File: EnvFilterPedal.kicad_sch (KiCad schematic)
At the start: 19 parts, among them U101 TL074

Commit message: schematic 1st pass
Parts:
- added C105, C106, C108, C109, C114, C115: 100n, symbol Device:C
- added C107: 4n7, symbol Device:C
- added C110, C112, C117, C118: 1n, symbol Device:C
- added C111, C113, C116, C119, C120: 1u, symbol Device:C
- added C121: 100u, Capacitor_THT:CP_Radial_D5.0mm_P2.00mm, symbol Device:C_Polarized_US
- added C122: 470p, Capacitor_SMD:C_0805_2012Metric, symbol Device:C
- added C123, C124: 470u, Capacitor_THT:CP_Radial_D5.0mm_P2.00mm, symbol Device:C_Polarized_US
- added D105, D106: 1N4148W, Diode_SMD:D_SOD-123, symbol Diode:1N4148W
- added D107: PMEG3030, Diode_SMD:D_SOD-123, symbol Device:D_Schottky
- added L101: 68uH, Inductor_SMD:L_TDK_VLS6045EX_VLS6045AF, symbol Device:L
- added Q101, Q102: BC857, Package_TO_SOT_SMD:SOT-23, symbol Transistor_BJT:BC857
- added R110, R111: 15k, symbol Device:R_US
- added R112, R113, R145, R146: 100k, symbol Device:R_US
- added R114: 2k2, symbol Device:R_US
- added R115: 470k, symbol Device:R_US
- added R116, R117, R126, R130, R131, R139: 4k7, symbol Device:R_US
- added R118, R128, R132, R140: 22k, symbol Device:R_US
- added R119, R120, R123, R127, R133, R138, R143, R144: 33k, symbol Device:R_US
- added R121, R122, R124, R125, R134, R135, R136, R137: 1k, symbol Device:R_US
- added R129: 10k, symbol Device:R_US
- added R141, R142: 47k, symbol Device:R_US
- added R147: 470, symbol Device:R_US
- added R148: 0.24R, Resistor_SMD:R_0805_2012Metric, symbol Device:R_US
- added R149: 51k, Resistor_SMD:R_0805_2012Metric, symbol Device:R_US
- added R150: 8k2, Resistor_SMD:R_0805_2012Metric, symbol Device:R_US
- added RV102, RV103, RV104: 10kB, symbol Device:R_Potentiometer_US
- added RV105: 100kB, symbol Device:R_Potentiometer_US
- added RV106: 100kA, symbol Device:R_Potentiometer_US
- added U102: TL074, symbol Amplifier_Operational:TL074
- added U103, U104: LM13700, symbol Amplifier_Operational:LM13700
- added U105: AZ34063U, Package_SO:SO-8_3.9x4.9mm_P1.27mm, symbol Regulator_Switching:AZ34063U
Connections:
- net +9V: now also C105.1, C108.1, C114.1, C121.1, R110.1, R148.1, U102.4 (V+), U103.11 (V+), U104.11 (V+), U105.6 (VCC)
- net -9V: now also C106.1, C109.1, C115.1, C122.2, C123.2, C124.2, D107.2 (A), R111.2, R115.2, R118.2, R128.2, R132.2, R140.2, R150.2, U102.11 (V-), U103.6 (V-), U104.6 (V-), U105.4 (GND)
- net ENV: now also RV102.1
- net FX_IN: now also C116.1, C117.2; no longer C103.1
- net GND: now also C105.2, C106.2, C108.2, C109.2, C112.2, C114.2, C115.2, C121.2, C123.1, C124.1, L101.2, Q101.1 (B), R114.2, R121.1, R122.1, R124.1, R125.1, R130.2, R134.1, R135.1, R136.1, R137.1, R146.1, R149.1, RV102.3, RV104.1, RV105.2, RV106.1, U102.12 (+), U102.5 (+)
- new net: R113.1, RV103.2
- new net: Q102.1 (B), R112.2, R113.2, R114.1
- new net: R131.2, U104.16
- new net: R133.1, R135.2, U104.13 (-)
- new net: R141.2, R143.1, RV105.1
- new net: R143.2, R144.2, R145.1, U102.13 (-)
- new net: C117.1, U104.10, U104.12
- new net: C119.1, R132.1, U104.9
- new net: C110.1, U103.5, U103.7
- new net: C110.2, D105.2 (A), D106.1 (K), R129.1, U102.8
- new net: C111.2, R119.2, R123.1
- new net: R123.2, R124.2, R127.1, U103.13 (-)
- new net: RV104.2, U102.10 (+)
- new net: R136.2, R138.1, U104.4 (-)
- new net: D105.1 (K), D106.2 (A), R129.2, R130.1, U102.9 (-)
- new net: C116.2, R120.1
- new net: R119.1, R120.2, R121.2, U103.4 (-)
- new net: C107.2, Q102.3 (C), R115.1, U102.6 (-)
- new net: C107.1, R116.2, U102.7
- new net: R112.1, U102.1, U102.2 (-)
- new net: RV102.2, U102.3 (+)
- new net: R126.1, U103.16
- new net: R146.2, R147.1, RV106.2
- new net: R145.2, RV106.3, U102.14
- new net: R142.2, R144.1, RV105.3
- new net: C112.1, U103.10, U103.12
- new net: R134.2, U104.14 (+)
- new net: Q101.2 (E), Q102.2 (E), R116.1
- new net: R139.2, U104.1
- new net: R137.2, U104.3 (+)
- new net: C118.1, U104.5, U104.7
- new net: R110.2, RV103.1
- new net: C120.1, R140.1, U104.8
- new net: C113.1, R128.1, U103.9
- new net: R117.1, U103.1
- new net: R122.2, U103.3 (+)
- new net: C111.1, R118.1, U103.8
- new net: R149.2, R150.1, U105.5 (FB)
- new net: R125.2, U103.14 (+)
- new net: R111.1, RV103.3
- new net: C122.1, U105.3 (CAP)
- new net ENV_IN: C103.1
- new net FX_OUT: R147.2
- new net HP1: C118.2, C119.2, R133.2
- new net HP_OUT: C120.2, R138.2, R141.1
- new net Iabc: Q101.3 (C), R117.2, R126.2, R131.1, R139.1
- new net LP_OUT: C113.2, R127.2, R142.1, RV104.3
- new net SWC: R148.2, U105.1 (SWC), U105.7 (Sense), U105.8 (DRC)
- new net SWE: D107.1 (K), L101.1, U105.2 (SWE)
- no-connect marks 0 -> 4
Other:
- note added: "Cutoff freq."
- note added: "Depth"
- note added: "Filter Mix"
- note added: "High Pass Section"
- note added: "Low Pass Section"
- note added: "OTA control current source"
- note added: "Resonance"
- note added: "Volume"

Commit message: footprints assigned
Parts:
- C101, C102, C103, C104, C105, C106, C107, C108, C109, C110, C111, C112, C113, C114, C115, C116, C117, C118, C119, C120: footprint (none) -> Capacitor_SMD:C_0805_2012Metric
- R101, R102, R103, R104, R105, R106, R107, R108, R109, R110, R111, R112, R113, R114, R115, R116, R117, R118, R119, R120, R121, R122, R123, R124, R125, R126, R127, R128, R129, R130, R131, R132, R133, R134, R135, R136, R137, R138, R139, R140, R141, R142, R143, R144, R145, R146, R147: footprint (none) -> Resistor_SMD:R_0805_2012Metric
- RV101, RV102, RV103, RV104, RV105, RV106: footprint (none) -> Potentiometer_THT:Potentiometer_Alpha_RV16AF_42_VeryLong
- U101, U102: footprint (none) -> Package_SO:SOIC-14_3.9x8.7mm_P1.27mm
- U103, U104: footprint (none) -> Package_SO:SOIC-16_3.9x9.9mm_P1.27mm
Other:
- note added: "Inverting SMPS"
- note added: "NOTE: this filter is based on the 2-pole resonant filter from my poly synth which in turn is based on the Korg MS-20 filter. I've swapped the op-amp current to voltage stages from those designs in favor of the LM13700's built-in darlington buffers. If spice can be trusted this circuit is almost identical in practice."
- note added: "Output Mixer"
- moved on the sheet: C121, C122, C123, C124, D107, L101, R148, R149, R150, U105

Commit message: rev 1 gerber
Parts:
- added C125: 10n, Capacitor_SMD:C_0805_2012Metric, symbol Device:C
- added D108: LED, LED_THT:LED_D3.0mm, symbol Device:LED
- added J101: ScopeGroundLoop, Connector:THT_GND_WIRE, symbol Connector:ScopeGroundLoop
- added J102: IO, Connector_PinHeader_2.54mm:PinHeader_1x05_P2.54mm_Vertical, symbol Connector:Conn_01x05_Pin
- added R151: 100k, Resistor_SMD:R_0805_2012Metric, symbol Device:R_US
- added R154: 4k7, Resistor_SMD:R_0805_2012Metric, symbol Device:R_US
- added TP101: In, TestPoint:TestPoint_THTPad_D2.0mm_Drill1.0mm_VAL, symbol Connector:TestPoint
- added TP102: Out, TestPoint:TestPoint_THTPad_D2.0mm_Drill1.0mm_VAL, symbol Connector:TestPoint
- added TP103: HP, TestPoint:TestPoint_THTPad_D2.0mm_Drill1.0mm_VAL, symbol Connector:TestPoint
- added TP104: LP, TestPoint:TestPoint_THTPad_D2.0mm_Drill1.0mm_VAL, symbol Connector:TestPoint
- added TP105: ENV, TestPoint:TestPoint_THTPad_D2.0mm_Drill1.0mm_VAL, symbol Connector:TestPoint
- added TP106: ENV_IN, TestPoint:TestPoint_THTPad_D2.0mm_Drill1.0mm_VAL, symbol Connector:TestPoint
- added TP107: HC, TestPoint:TestPoint_THTPad_D2.0mm_Drill1.0mm_VAL, symbol Connector:TestPoint
- added TP108: FR, TestPoint:TestPoint_THTPad_D2.0mm_Drill1.0mm_VAL, symbol Connector:TestPoint
- R106: value 820 -> 680
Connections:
- net +9V: now also J102.5 (Pin_5), R154.1
- net ENV: now also RV103.3, U101.7, TP105.1; no longer RV102.1, U101.14
- net ENV_IN: now also J102.3 (Pin_3), TP106.1
- net EnvCap: now also R151.1; no longer U101.12 (+)
- net FX_IN: now also J102.2 (Pin_2), TP101.1
- net FX_OUT: now also J102.1 (Pin_1), TP102.1
- net FullRect: now also TP108.1
- net GND: now also RV103.1, U101.12 (+), U102.10 (+), C125.2, D108.1 (K), J101.1, J102.4 (Pin_4); no longer RV102.3, U101.5 (+), U102.12 (+)
- net HP_OUT: now also TP103.1
- net HardClip: now also TP107.1
- net LP_OUT: now also TP104.1
- net at R113.1: now also RV102.2; no longer RV103.2
- net vBase: now reaches Q102.1 (B), R112.2, R113.2, R114.1
- net at R104.2, R105.1: now also U101.13 (-); no longer U101.6 (-)
- net at D103.2 (A): now also U101.14; no longer U101.7
- net at R143.2, R144.2, R145.1: now also U102.9 (-); no longer U102.13 (-)
- net at C110.2, D105.2 (A), D106.1 (K)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: now also U102.14; no longer U102.8
- net at R108.1, R109.1: now also U101.6 (-); no longer U101.13 (-)
- net at RV104.2: now also U102.12 (+); no longer U102.10 (+)
- net at D105.1 (K), D106.2 (A), R129.2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: now also U102.13 (-); no longer U102.9 (-)
- net at U102.3 (+): no longer RV102.2
- net at R145.2, RV106.3: now also U102.8; no longer U102.14
- net ComEmmiter: now reaches Q101.2 (E), Q102.2 (E), R116.1
- net at R110.2: now also RV102.3; no longer RV103.1
- net at R111.1: now also RV102.1; no longer RV103.3
- new net: C125.1, R151.2, U101.5 (+)
- new net: D108.2 (A), R154.2
- new net: R112.1, RV103.2
- now unconnected: U102.1, U102.2 (-)
- no-connect marks 4 -> 7
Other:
- note added: "Header and Test Points"
- moved on the sheet: C104, C105, C106, C107, C121, C122, C123, C124, D104, D107, L101, Q101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

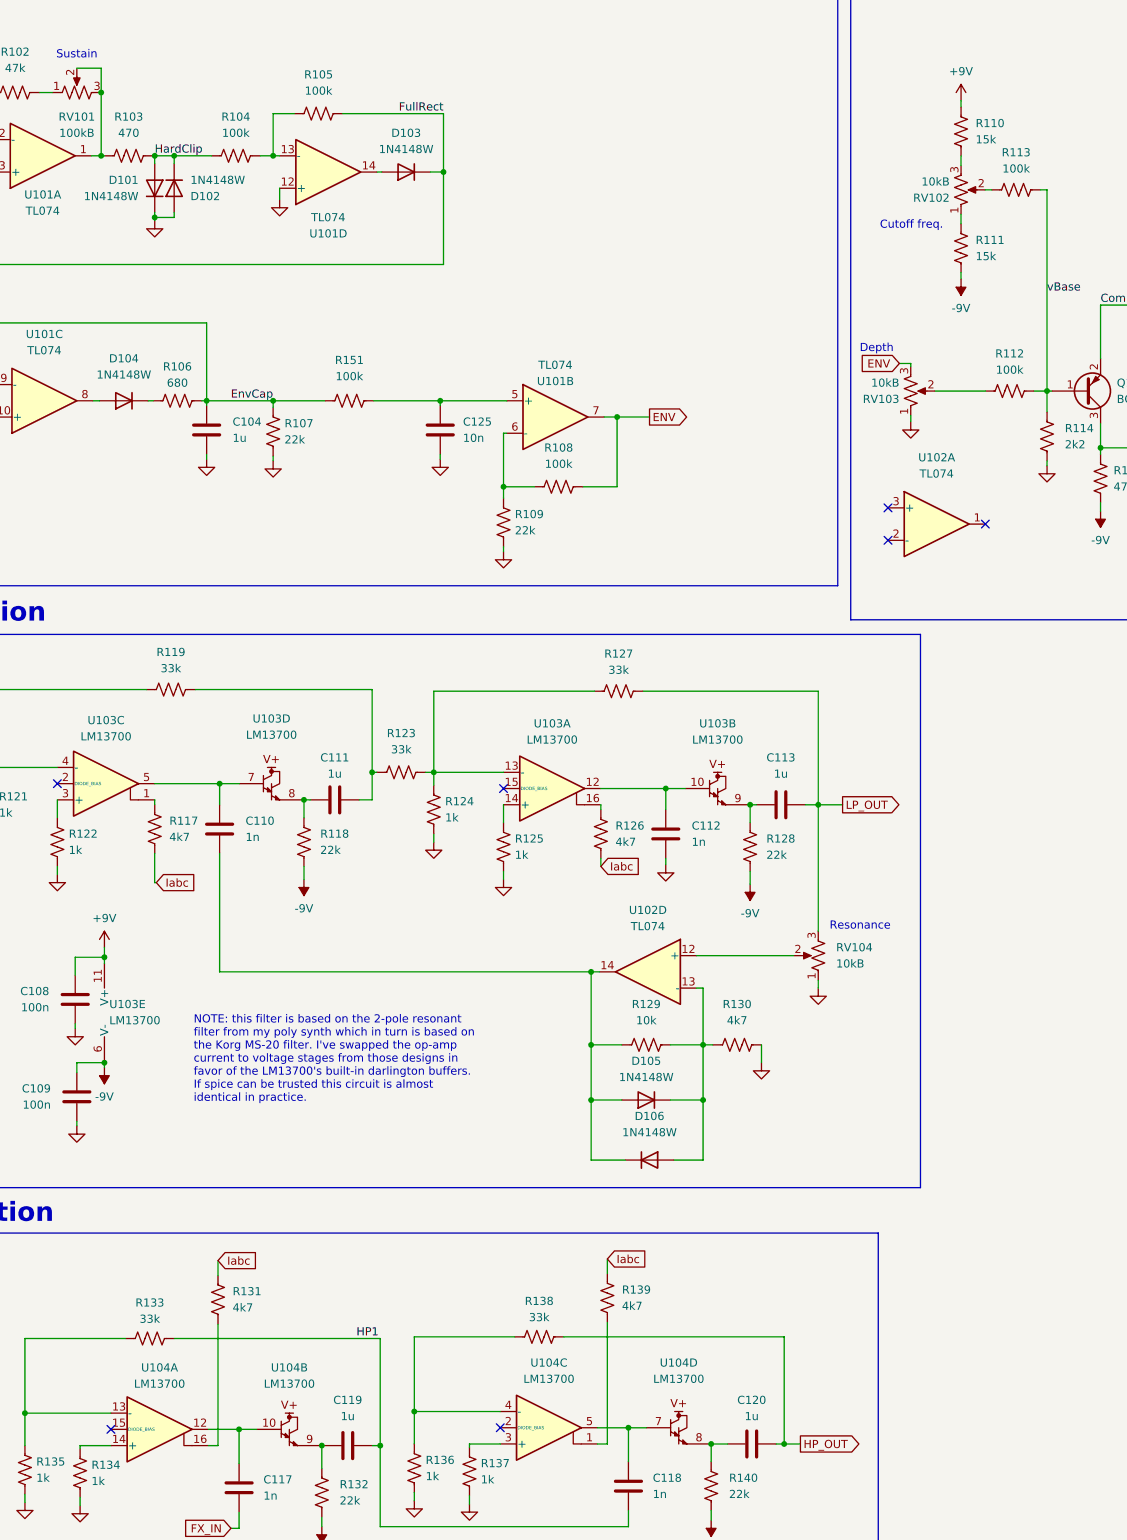
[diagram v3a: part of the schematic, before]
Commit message: filter value tweaks
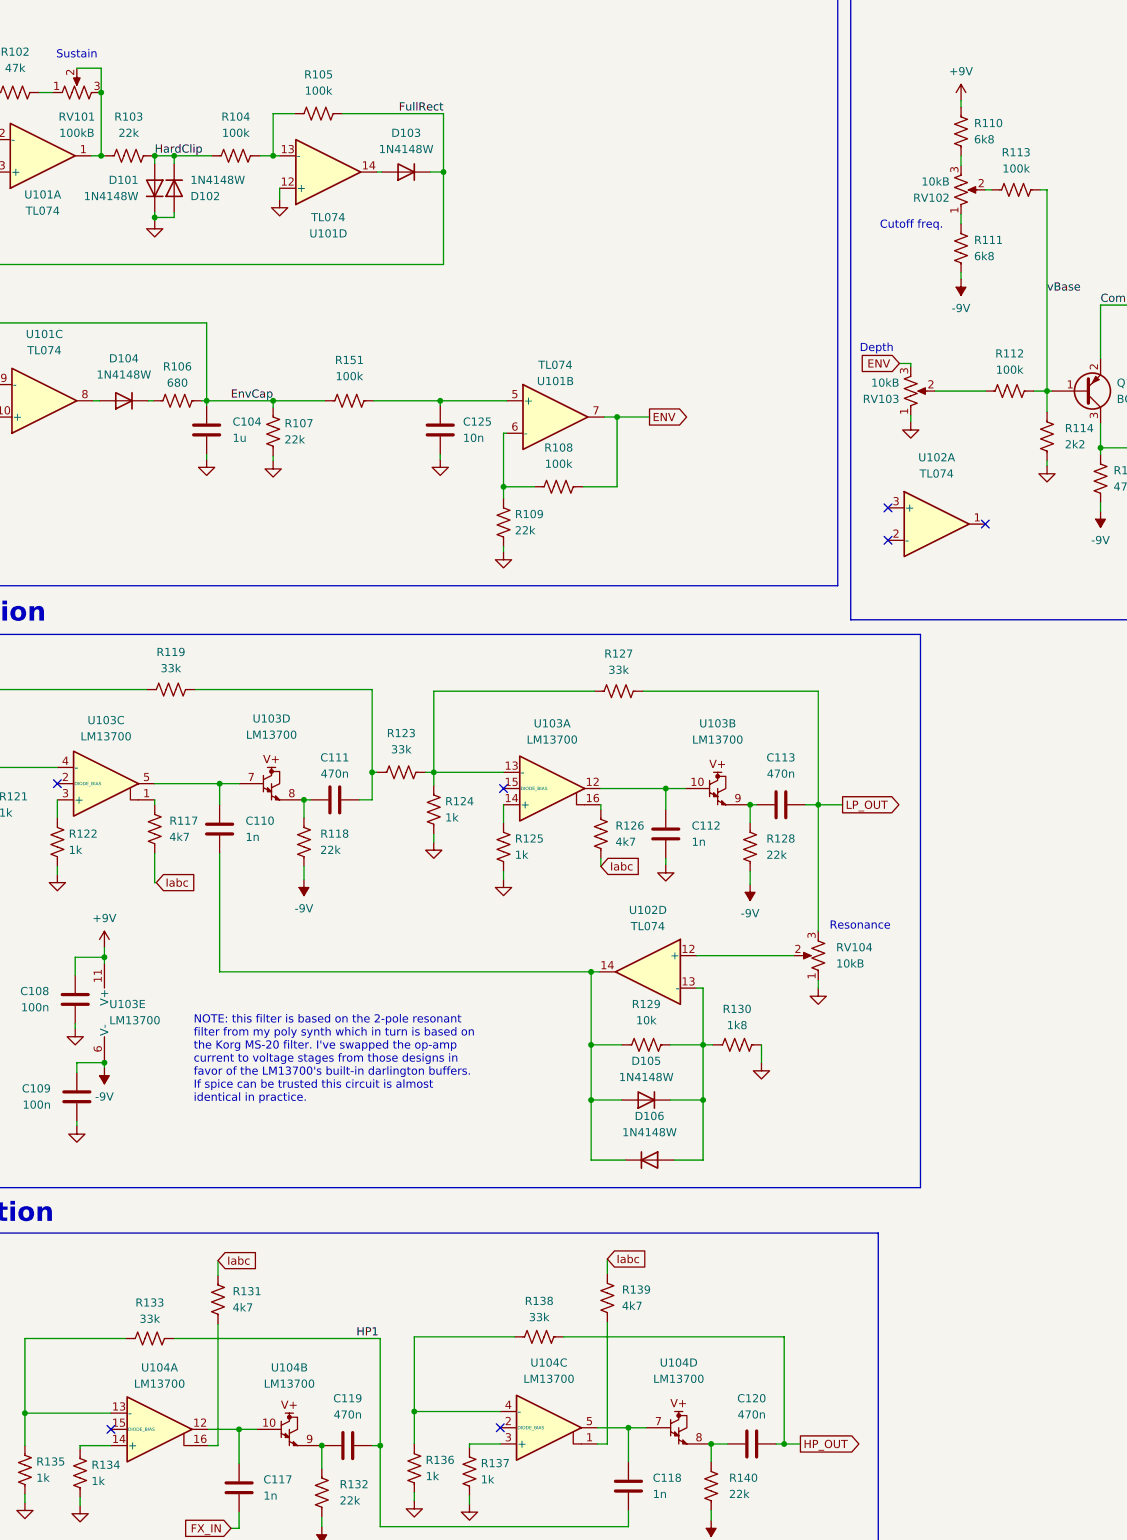
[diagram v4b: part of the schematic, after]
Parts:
- C111, C113, C119, C120: value 1u -> 470n
- R103: value 470 -> 22k
- R110, R111: value 15k -> 6k8
- R130: value 4k7 -> 1k8
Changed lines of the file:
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@@
 		(fields_autoplaced yes)
 		(property "Reference" "R110"
-			(at 200.914 42.9259 0)
+			(at 200.66 42.9259 0)
 			(effects
 				(font
@@
 			)
 		)
-		(property "Value" "15k"
-			(at 200.914 45.4659 0)
+		(property "Value" "6k8"
+			(at 200.66 45.4659 0)
 			(effects
 				(font
@@
 		(fields_autoplaced yes)
 		(property "Reference" "C119"
-			(at 102.616 242.824 90)
+			(at 102.616 242.57 90)
 			(effects
 				(font
@@
 			)
 		)
-		(property "Value" "1u"
-			(at 102.616 245.364 90)
+		(property "Value" "470n"
+			(at 102.616 245.11 90)
 			(effects
 				(font
@@
 			)
 		)
-		(property "Value" "470"
+		(property "Value" "22k"
 			(at 68.326 44.45 90)
 			(effects
@@
 			)
 		)
-		(property "Value" "1u"
+		(property "Value" "470n"
 			(at 170.434 144.78 90)
 			(effects
@@
 		(fields_autoplaced yes)
 		(property "Reference" "R111"
-			(at 200.914 61.2139 0)
+			(at 200.66 61.2139 0)
 			(effects
 				(font
@@
 			)
 		)
-		(property "Value" "15k"
-			(at 200.914 63.7539 0)
+		(property "Value" "6k8"
+			(at 200.66 63.7539 0)
 			(effects
 				(font
@@
 			)
 		)
-		(property "Value" "1u"
+		(property "Value" "470n"
 			(at 100.584 144.78 90)
 			(effects
@@
 		(fields_autoplaced yes)
 		(property "Reference" "R130"
-			(at 163.576 180.848 90)
+			(at 163.576 181.61 90)
 			(effects
 				(font
@@
 			)
 		)
-		(property "Value" "4k7"
-			(at 163.576 183.388 90)
+		(property "Value" "1k8"
+			(at 163.576 184.15 90)
 			(effects
 				(font
@@
 		(fields_autoplaced yes)
 		(property "Reference" "C120"
-			(at 165.862 242.824 90)
+			(at 165.862 242.57 90)
 			(effects
 				(font
@@
 			)
 		)
-		(property "Value" "1u"
-			(at 165.862 245.364 90)
+		(property "Value" "470n"
+			(at 165.862 245.11 90)
 			(effects
 				(font

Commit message: rev2 simulation stuff
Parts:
- removed C105, C106, C108, C109, C114, C115: 100n, Capacitor_SMD:C_0805_2012Metric, symbol Device:C
- removed C110, C112, C117, C118: 1n, Capacitor_SMD:C_0805_2012Metric, symbol Device:C
- removed C111, C113, C119, C120: 470n, Capacitor_SMD:C_0805_2012Metric, symbol Device:C
- removed C116: 1u, Capacitor_SMD:C_0805_2012Metric, symbol Device:C
- removed C125: 10n, Capacitor_SMD:C_0805_2012Metric, symbol Device:C
- removed D104, D105, D106: 1N4148W, Diode_SMD:D_SOD-123, symbol Diode:1N4148W
- removed R117, R126, R131, R139: 4k7, Resistor_SMD:R_0805_2012Metric, symbol Device:R_US
- removed R118, R128, R132, R140: 22k, Resistor_SMD:R_0805_2012Metric, symbol Device:R_US
- removed R119, R120, R123, R127, R133, R138, R143, R144: 33k, Resistor_SMD:R_0805_2012Metric, symbol Device:R_US
- removed R121, R122, R124, R125, R134, R135, R136, R137: 1k, Resistor_SMD:R_0805_2012Metric, symbol Device:R_US
- removed R129: 10k, Resistor_SMD:R_0805_2012Metric, symbol Device:R_US
- removed R130: 1k8, Resistor_SMD:R_0805_2012Metric, symbol Device:R_US
- removed R141, R142: 47k, Resistor_SMD:R_0805_2012Metric, symbol Device:R_US
- removed R145, R146, R151: 100k, Resistor_SMD:R_0805_2012Metric, symbol Device:R_US
- removed R147: 470, Resistor_SMD:R_0805_2012Metric, symbol Device:R_US
- removed RV101, RV105: 100kB, Potentiometer_THT:Potentiometer_Alpha_RV16AF_42_VeryLong, symbol Device:R_Potentiometer_US
- removed RV104: 10kB, Potentiometer_THT:Potentiometer_Alpha_RV16AF_42_VeryLong, symbol Device:R_Potentiometer_US
- removed RV106: 100kA, Potentiometer_THT:Potentiometer_Alpha_RV16AF_42_VeryLong, symbol Device:R_Potentiometer_US
- removed TP107: HC, TestPoint:TestPoint_THTPad_D2.0mm_Drill1.0mm_VAL, symbol Connector:TestPoint
- removed U102: TL074, Package_SO:SOIC-14_3.9x8.7mm_P1.27mm, symbol Amplifier_Operational:TL074
- removed U103, U104: LM13700, Package_SO:SOIC-16_3.9x9.9mm_P1.27mm, symbol Amplifier_Operational:LM13700
- added C105: 470u, Capacitor_THT:CP_Radial_D5.0mm_P2.00mm, symbol Device:C_Polarized_US
- added FB101: 90R, Inductor_SMD:L_0805_2012Metric, symbol Device:FerriteBead
- R101, R103: value 22k -> 100k
- R102: value 47k -> 100k
- R106: value 680 -> 1k
- R109: value 22k -> 6k8
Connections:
- net -9V: now also C105.2, FB101.2; no longer C122.2, C123.2, C124.2, D107.2 (A), R150.2, U105.4 (GND)
- net FullRect: now also R103.2, U101.1, U101.12 (+); no longer D103.1 (K), R105.2, U101.10 (+)
- net GND: now also U101.10 (+), C105.1; no longer D101.1 (K), D102.2 (A), U101.12 (+)
- net at U101.5 (+): now also C104.1, R106.2, R107.1, U101.13 (-)
- net at R101.1: now also D102.2 (A), R102.1, R105.2; no longer C103.2
- net at R101.2, U101.2 (-): now also R102.2, R103.1; no longer R102.1
- net at R104.2, R105.1: now also D101.1 (K), U101.9 (-); no longer U101.13 (-)
- net at R106.1: now also D103.1 (K)
- net at U101.8: now also D101.2 (A), D102.1 (K)
- removed net EnvCap: C104.1, R106.2, R107.1, U101.9 (-)
- removed net HardClip: D101.2 (A), D102.1 (K), R103.2, R104.1
- new net: C122.2, C123.2, C124.2, D107.2 (A), FB101.1, R150.2, U105.4 (GND)
- new net: C103.2, R104.1
- no-connect marks 7 -> 0
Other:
- note removed: "Filter Mix"
- note removed: "High Pass Section"
- note removed: "Low Pass Section"
- note removed: "NOTE: this filter is based on the 2-pole resonant filter from my poly synth which in turn is based on the Korg MS-20 filter. I've swapped the op-amp current to voltage stages from those designs in favor of the LM13700's built-in darlington buffers. If spice can be trusted this circuit is almost identical in practice."
- note removed: "Resonance"
- note removed: "Sustain"
- note removed: "Volume"
- moved on the sheet: C101, C102, C103, C107, Q101, Q102, R104, R105, R110, R111, R112, R113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
